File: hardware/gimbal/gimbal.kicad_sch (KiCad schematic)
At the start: 5 parts

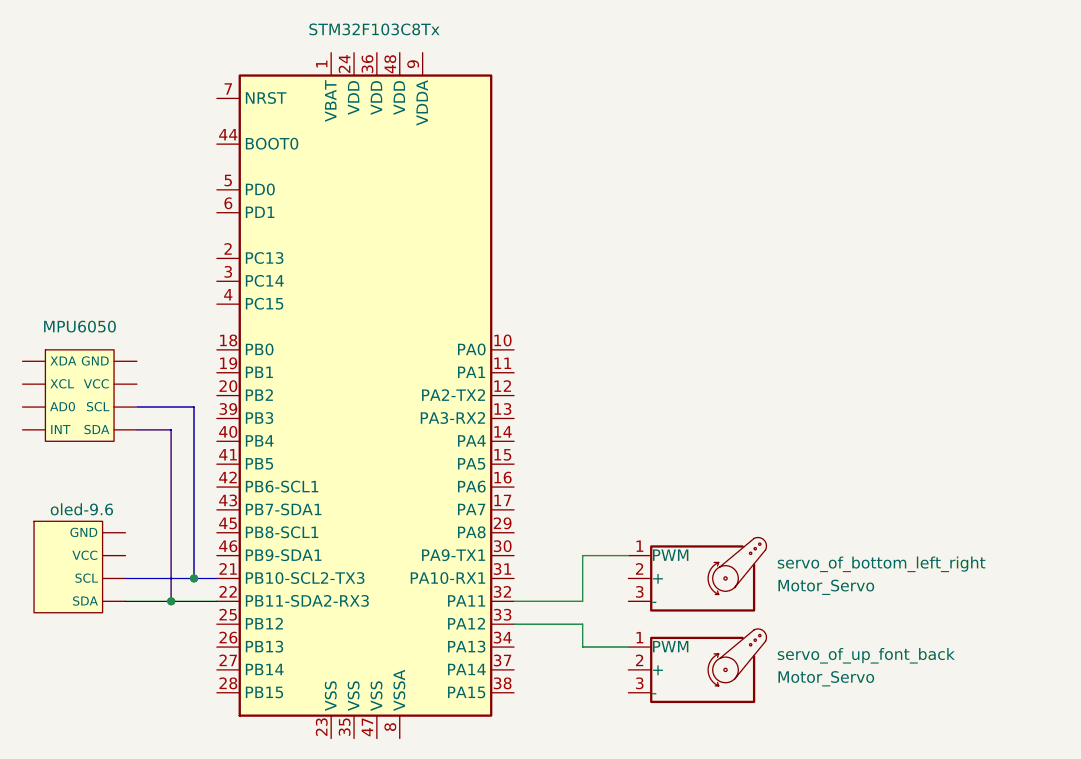
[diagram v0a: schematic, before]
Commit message: fix pwm gpio to timer3 channel.
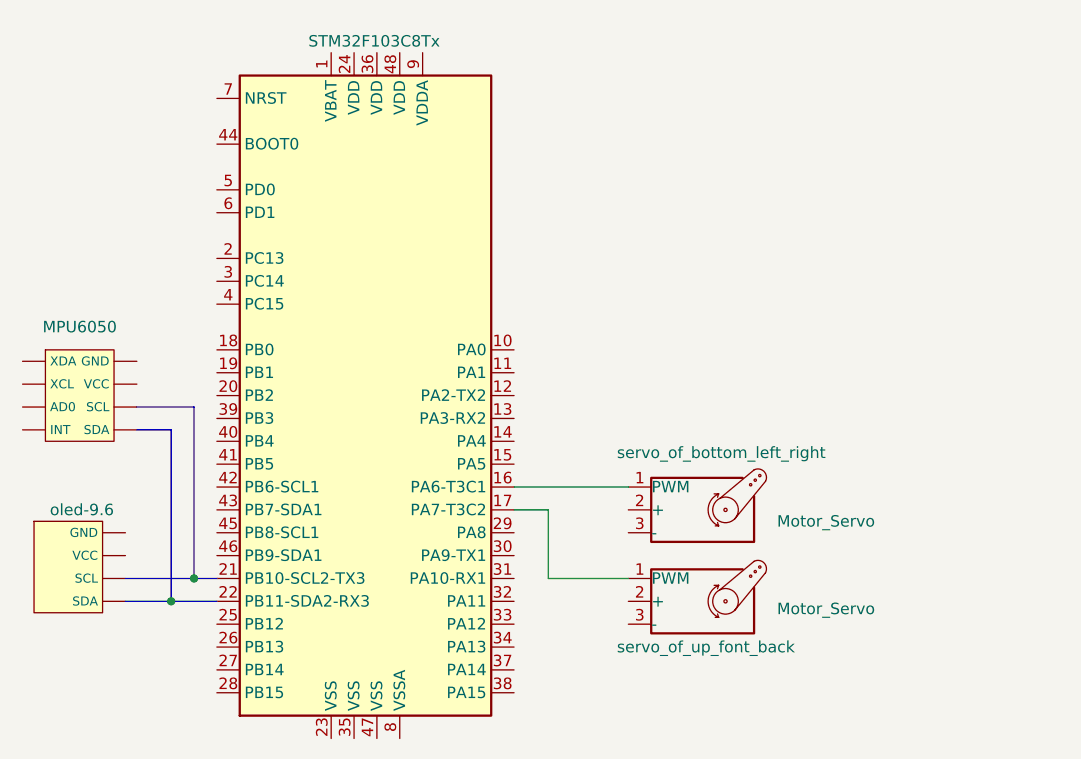
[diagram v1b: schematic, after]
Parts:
- removed U?: STM32F103C8Tx, Package_QFP:LQFP-48_7x7mm_P0.5mm, symbol MCU_ST_STM32F1:STM32F103C8Tx
- added U?: STM32F103C8Tx, Package_QFP:LQFP-48_7x7mm_P0.5mm, symbol MCU_ST_STM32F1:STM32F103C8Tx
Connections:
- net at servo_of_up_font_back.1 (PWM): now also U?.17 (PA7-T3C2)
- net at servo_of_bottom_left_right.1 (PWM): now also U?.16 (PA6-T3C1)
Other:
- moved on the sheet: servo_of_bottom_left_right, servo_of_up_font_back
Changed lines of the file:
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@@
   (junction (at 90.17 124.46) (diameter 0) (color 0 0 0 0)
+  )
+  (wire (pts (xy 128.27 114.3) (xy 132.08 114.3))
+    (stroke (width 0) (type default) (color 0 0 0 0))
   )
   (bus (pts (xy 92.71 102.87) (xy 92.71 121.92))
     (stroke (width 0) (type default) (color 0 0 0 0))
   )
-  (wire (pts (xy 135.89 119.38) (xy 140.97 119.38))
+  (wire (pts (xy 140.97 121.92) (xy 132.08 121.92))
+    (stroke (width 0) (type default) (color 0 0 0 0))
+  )
+  (wire (pts (xy 128.27 111.76) (xy 140.97 111.76))
+    (stroke (width 0) (type default) (color 0 0 0 0))
+  )
+  (wire (pts (xy 132.08 121.92) (xy 132.08 114.3))
     (stroke (width 0) (type default) (color 0 0 0 0))
   )
@@
     (stroke (width 0) (type default) (color 0 0 0 0))
   )
-  (wire (pts (xy 128.27 124.46) (xy 135.89 124.46))
-    (stroke (width 0) (type default) (color 0 0 0 0))
-  )
-  (wire (pts (xy 135.89 124.46) (xy 135.89 119.38))
-    (stroke (width 0) (type default) (color 0 0 0 0))
-  )
   (bus (pts (xy 85.09 121.92) (xy 92.71 121.92))
     (stroke (width 0) (type default) (color 0 0 0 0))
@@
     (stroke (width 0) (type default) (color 0 0 0 0))
   )
-  (wire (pts (xy 128.27 127) (xy 135.89 127))
-    (stroke (width 0) (type default) (color 0 0 0 0))
-  )
-  (wire (pts (xy 135.89 129.54) (xy 140.97 129.54))
-    (stroke (width 0) (type default) (color 0 0 0 0))
-  )
   (bus (pts (xy 90.17 124.46) (xy 95.25 124.46))
-    (stroke (width 0) (type default) (color 0 0 0 0))
-  )
-  (wire (pts (xy 135.89 127) (xy 135.89 129.54))
     (stroke (width 0) (type default) (color 0 0 0 0))
   )
@@
     (pin "")
   )
-  (symbol (lib_id "Motor:Motor_Servo") (at 148.59 132.08 0) (unit 1)
-    (in_bom yes) (on_board yes) (fields_autoplaced)
-    (property "Reference" "servo_of_up_font_back" (id 0) (at 157.48 130.3765 0)
+  (symbol (lib_id "Motor:Motor_Servo") (at 148.59 124.46 0) (unit 1)
+    (in_bom yes) (on_board yes)
+    (property "Reference" "servo_of_up_font_back" (id 0) (at 139.7 129.54 0)
       (effects (font (size 1.27 1.27)) (justify left))
     )
-    (property "Value" "Motor_Servo" (id 1) (at 157.48 132.9165 0)
+    (property "Value" "Motor_Servo" (id 1) (at 157.48 125.2965 0)
       (effects (font (size 1.27 1.27)) (justify left))
     )
-    (property "Footprint" "" (id 2) (at 148.59 136.906 0)
+    (property "Footprint" "" (id 2) (at 148.59 129.286 0)
       (effects (font (size 1.27 1.27)) hide)
     )
-    (property "Datasheet" "http://forums.parallax.com/uploads/attachments/46831/74481.png" (id 3) (at 148.59 136.906 0)
+    (property "Datasheet" "http://forums.parallax.com/uploads/attachments/46831/74481.png" (id 3) (at 148.59 129.286 0)
       (effects (font (size 1.27 1.27)) hide)
     )
@@
       (effects (font (size 1.27 1.27)) (justify left) hide)
     )
-    (property "Value" "STM32F103C8Tx" (id 1) (at 105.41 60.96 0)
+    (property "Value" "STM32F103C8Tx" (id 1) (at 105.41 62.23 0)
       (effects (font (size 1.27 1.27)) (justify left))
     )
@@
     (pin "9")
   )
-  (symbol (lib_id "Motor:Motor_Servo") (at 148.59 121.92 0) (unit 1)
-    (in_bom yes) (on_board yes) (fields_autoplaced)
-    (property "Reference" "servo_of_bottom_left_right" (id 0) (at 157.48 120.2165 0)
+  (symbol (lib_id "Motor:Motor_Servo") (at 148.59 114.3 0) (unit 1)
+    (in_bom yes) (on_board yes)
+    (property "Reference" "servo_of_bottom_left_right" (id 0) (at 139.7 107.95 0)
       (effects (font (size 1.27 1.27)) (justify left))
     )
-    (property "Value" "Motor_Servo" (id 1) (at 157.48 122.7565 0)
+    (property "Value" "Motor_Servo" (id 1) (at 157.48 115.57 0)
       (effects (font (size 1.27 1.27)) (justify left))
     )
-    (property "Footprint" "" (id 2) (at 148.59 126.746 0)
+    (property "Footprint" "" (id 2) (at 148.59 119.126 0)
       (effects (font (size 1.27 1.27)) hide)
     )
-    (property "Datasheet" "http://forums.parallax.com/uploads/attachments/46831/74481.png" (id 3) (at 148.59 126.746 0)
+    (property "Datasheet" "http://forums.parallax.com/uploads/attachments/46831/74481.png" (id 3) (at 148.59 119.126 0)
       (effects (font (size 1.27 1.27)) hide)
     )
@@
       (reference "U?") (unit 1) (value "oled-9.6") (footprint "")
     )
-    (path "/c02eeb0e-4b09-4b43-ad04-cdf13403d58a"
+    (path "/77528e43-19e9-4782-9deb-50cf2c1e01a6"
       (reference "U?") (unit 1) (value "STM32F103C8Tx") (footprint "Package_QFP:LQFP-48_7x7mm_P0.5mm")
     )
